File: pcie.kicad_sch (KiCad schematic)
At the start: 1 part

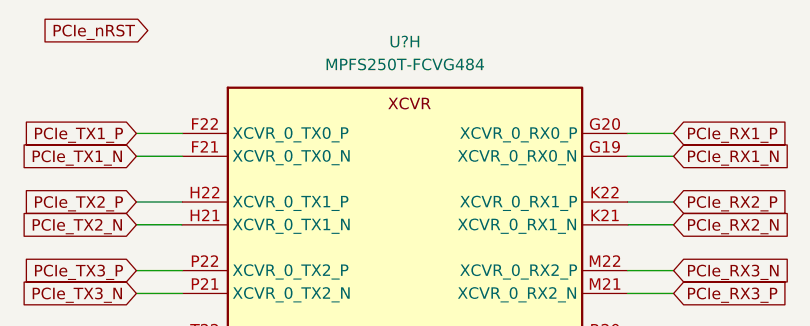
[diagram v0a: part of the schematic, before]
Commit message: [#52579] Connect CSI and DSI to CrossLink
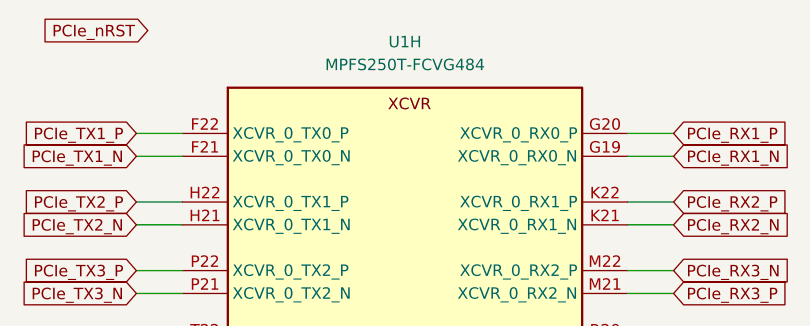
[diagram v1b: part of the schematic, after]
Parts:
- gave numbers to parts that had none: 1
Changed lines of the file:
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@@
   (symbol (lib_id "antmicroMicrocontrollers:MPFS250T-FCVG484") (at 121.92 73.66 0) (unit 8)
     (in_bom yes) (on_board yes) (fields_autoplaced)
-    (property "Reference" "U?" (id 0) (at 146.685 63.5 0)
+    (property "Reference" "U1" (id 0) (at 146.685 63.5 0)
       (effects (font (size 1.27 1.27) (thickness 0.15)))
     )

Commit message: [#52577] Clear annotations
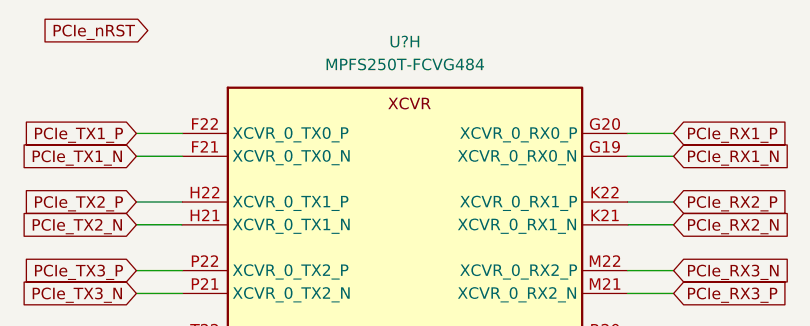
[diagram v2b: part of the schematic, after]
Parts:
- renumbered U1 to U?
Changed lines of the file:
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@@
   (symbol (lib_id "antmicroMicrocontrollers:MPFS250T-FCVG484") (at 121.92 73.66 0) (unit 8)
     (in_bom yes) (on_board yes) (fields_autoplaced)
-    (property "Reference" "U1" (id 0) (at 146.685 63.5 0)
+    (property "Reference" "U?" (id 0) (at 146.685 63.5 0)
       (effects (font (size 1.27 1.27) (thickness 0.15)))
     )

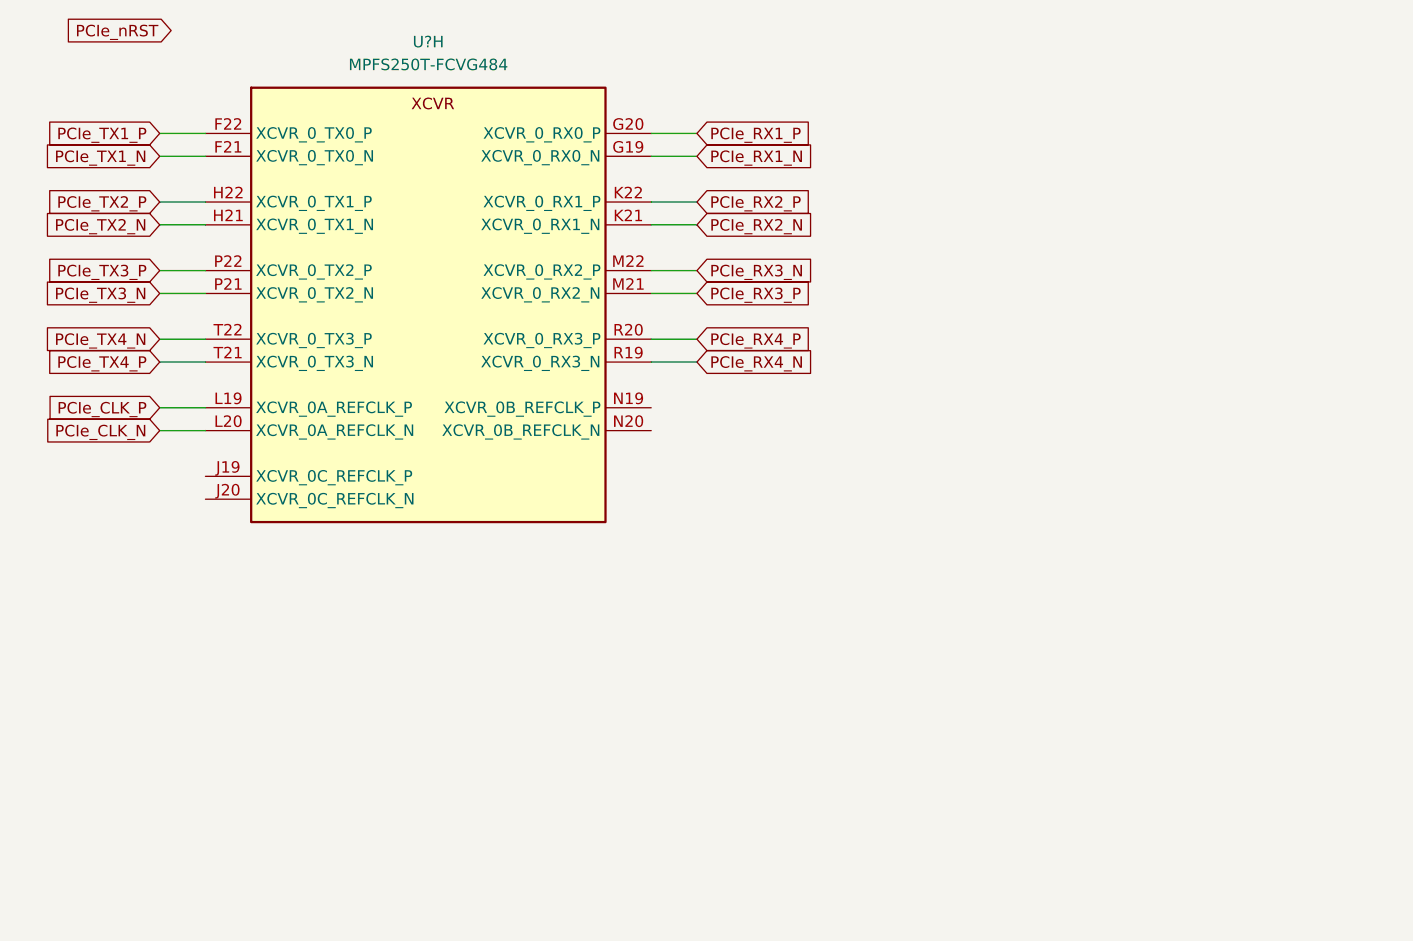
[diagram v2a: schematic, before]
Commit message: [#54084] Sheets cleanup
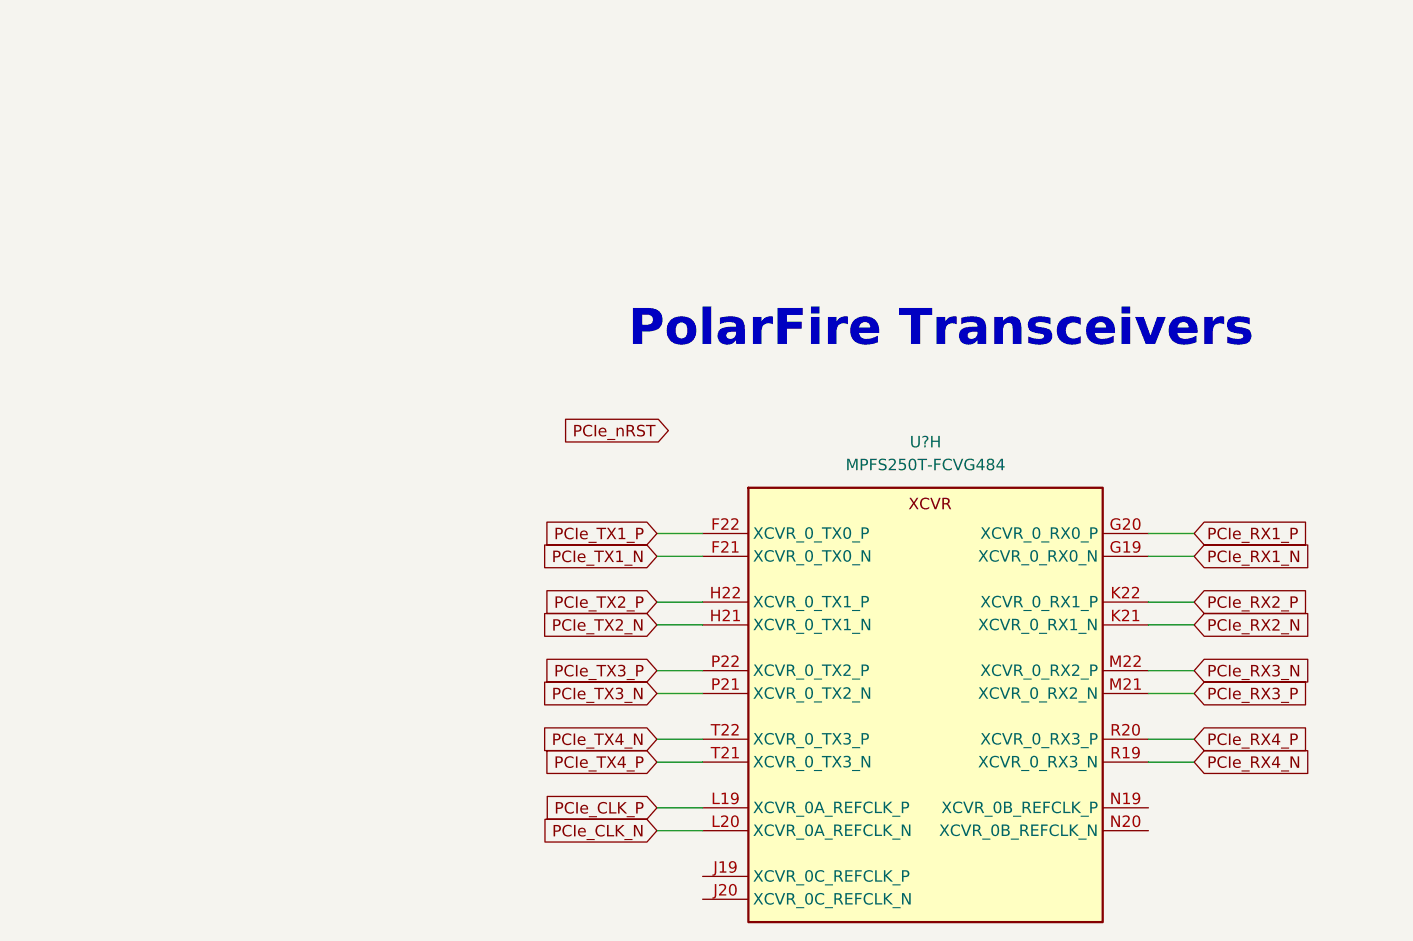
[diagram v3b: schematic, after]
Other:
- note added: "PolarFire Transceivers"
- company: (none) -> Antmicro Ltd
- title: (none) -> PolarFire SoM
- moved on the sheet: U?H

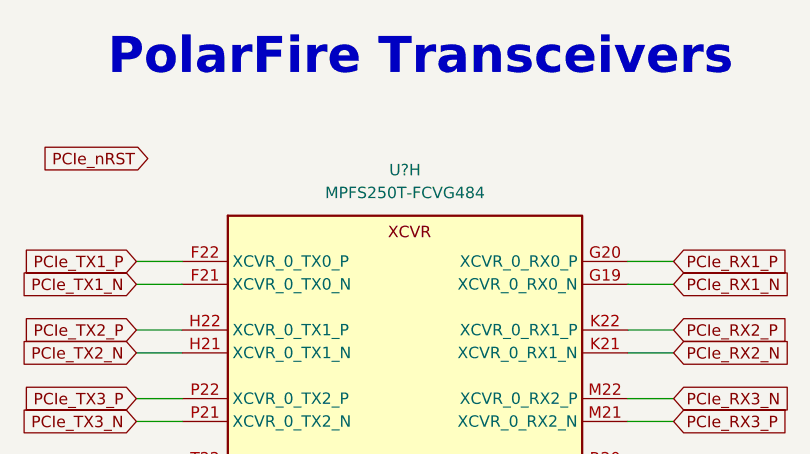
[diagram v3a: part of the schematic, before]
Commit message: [#54016] Place components to assess available space
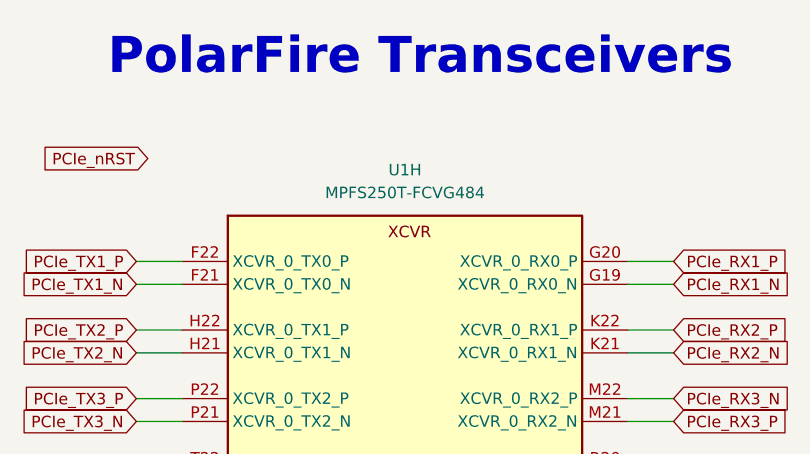
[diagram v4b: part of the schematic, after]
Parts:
- gave numbers to parts that had none: 1
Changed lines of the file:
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@@
   (symbol (lib_id "antmicroMicrocontrollers:MPFS250T-FCVG484") (at 177.165 118.11 0) (unit 8)
     (in_bom yes) (on_board yes) (fields_autoplaced)
-    (property "Reference" "U?" (id 0) (at 201.93 107.95 0)
+    (property "Reference" "U1" (id 0) (at 201.93 107.95 0)
       (effects (font (size 1.27 1.27) (thickness 0.15)))
     )
